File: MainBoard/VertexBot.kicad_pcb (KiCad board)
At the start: 2 copper layers, 115.6 x 107.8 mm, 70 parts, among them J1 Battery, J2 I2C Extension, J4 Left Motor, J5 Right Motor, J6 Led Strip, Q1 BSS138, Q2 BSS138, Q3 BSS138, SW1 SW_SPST, U1 DRV8830DGQR, U10 MAX4466 (LEFT), U11 MAX4466 (RIGHT), U12 ESP32-S3-CAM-B, U13 ESP32-S3-CAM-A, U14 MAX98357A, U2 DRV8830DGQR, U3 S13V30F5, U5 INMP441, U6 0.96 INCH OLED, U7 DRV5033AJxLPG, U8 DRV5033AJxLPG, U9 MPU 6050

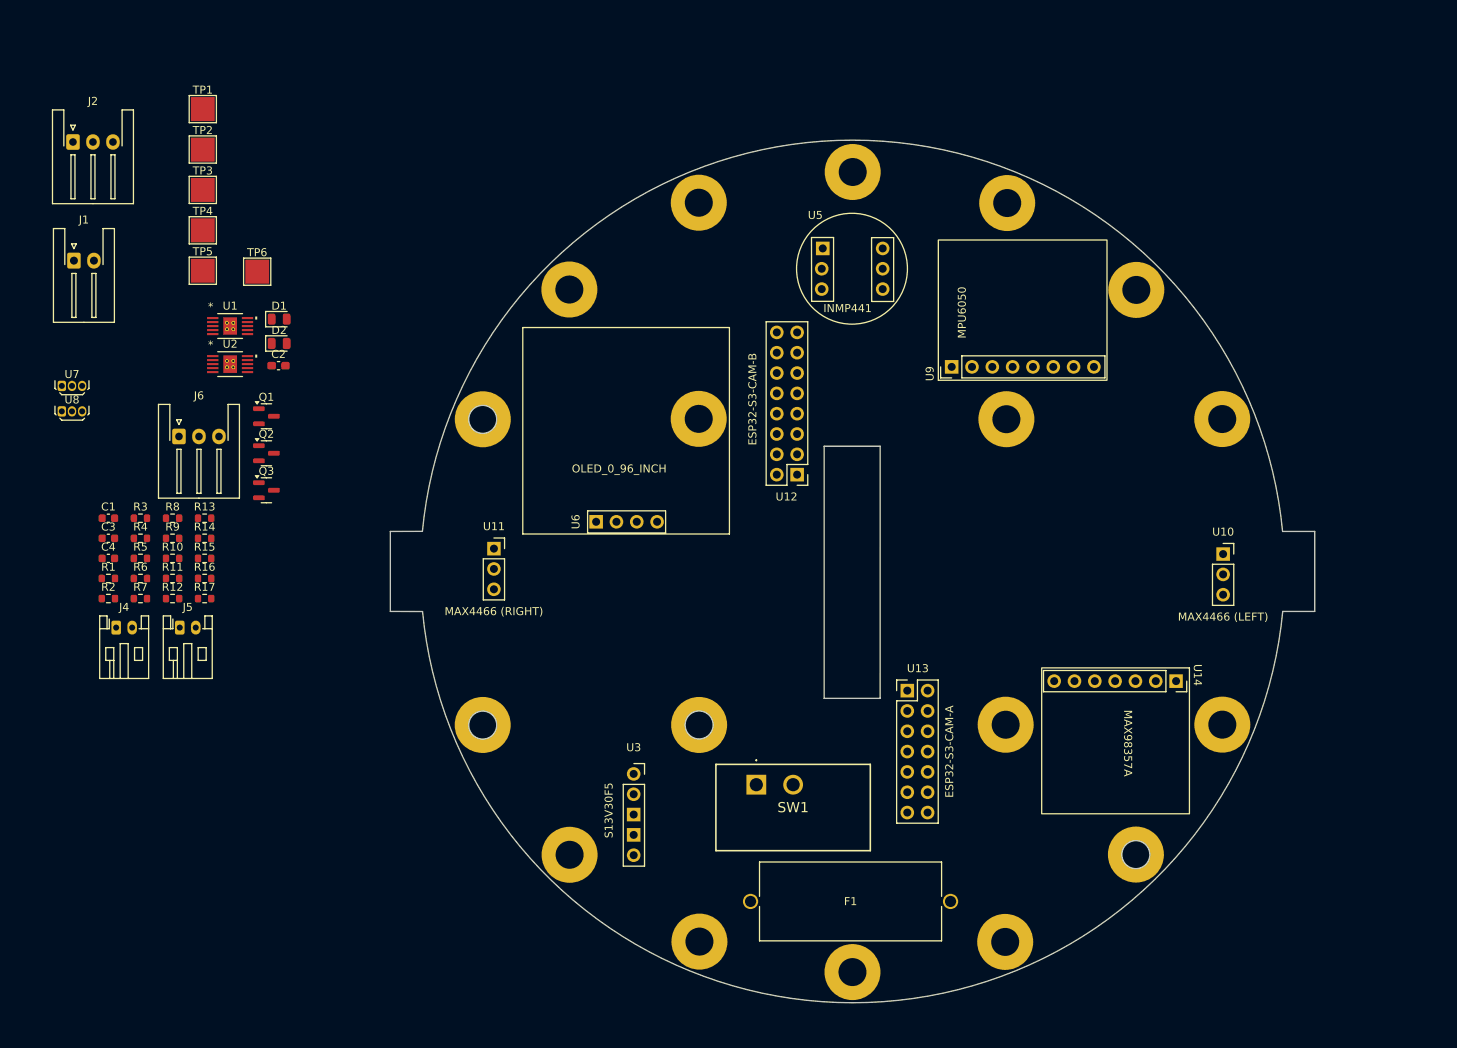
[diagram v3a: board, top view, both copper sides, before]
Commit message: Adjust DRV8830DGQR to allow thermal pad connect to GND Adjust some of the modules courtyard Fix mounting holes symbols to have connection
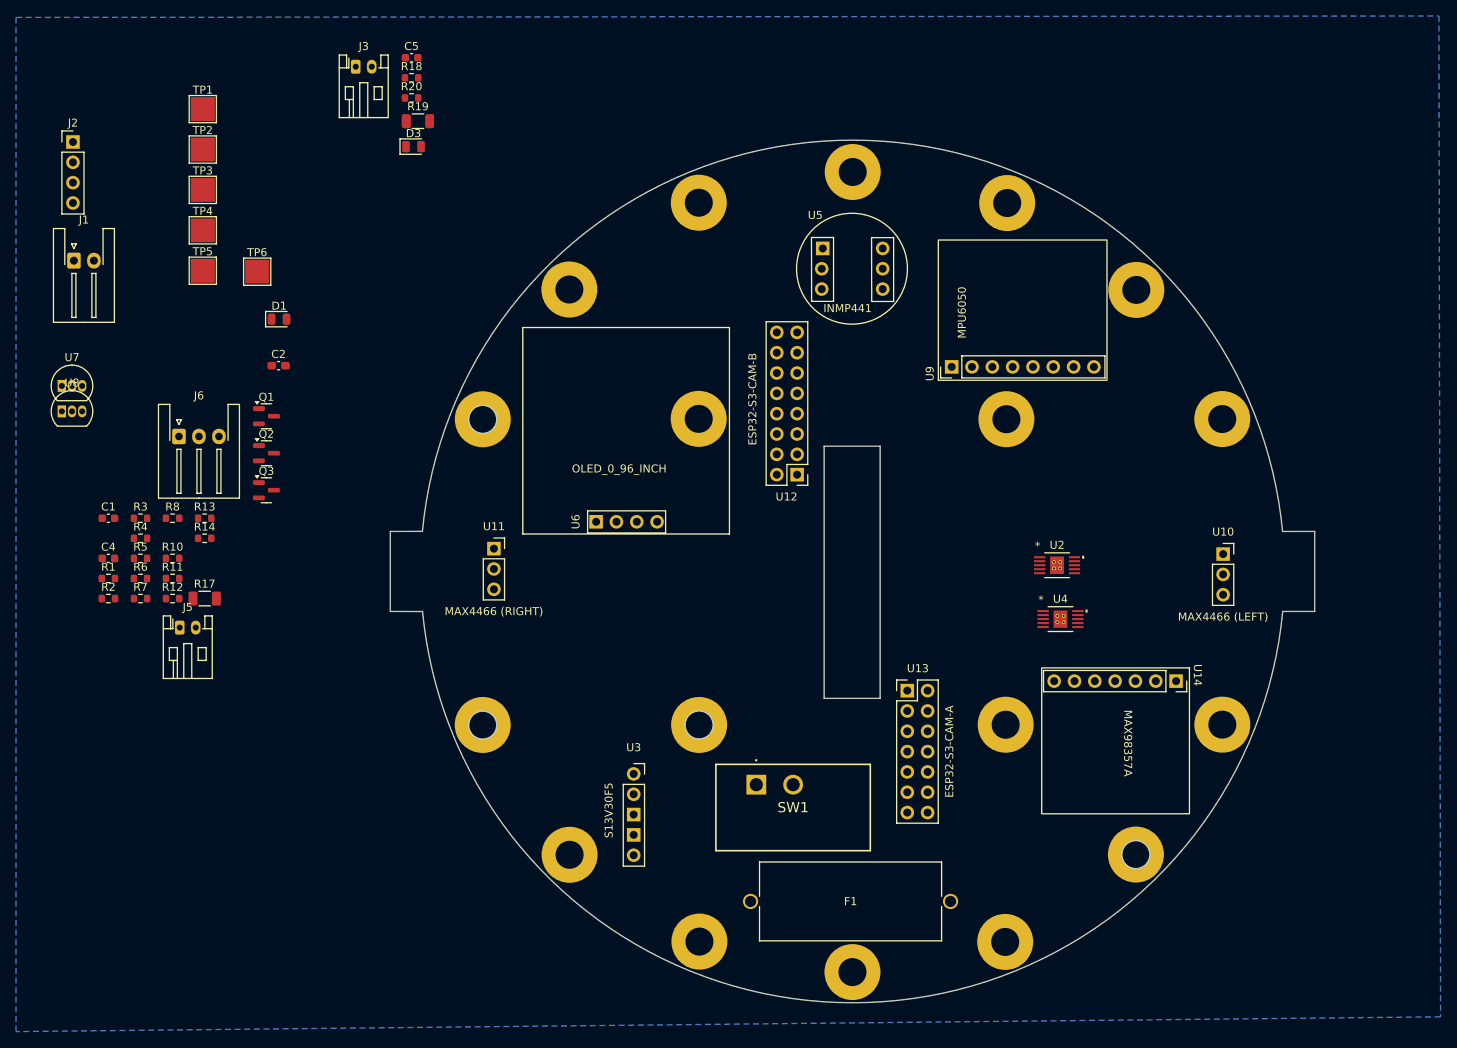
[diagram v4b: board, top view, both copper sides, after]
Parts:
- removed C3: 100nF, Capacitor_SMD:C_0603_1608Metric
- removed D2: LED, LED_SMD:LED_0805_2012Metric
- removed J4: Left Motor, Connector_JST:JST_PH_S2B-PH-K_1x02_P2.00mm_Horizontal
- removed R15: 1K, Resistor_SMD:R_0603_1608Metric
- removed R16, R9: 0.44, Resistor_SMD:R_0603_1608Metric
- removed U1: DRV8830DGQR, Vertex_Bot:DGQ10_2P18X1P72
- added C5: 100nF, Capacitor_SMD:C_0603_1608Metric, F.Cu at (65.1, 25.2)
- added D3: LED, LED_SMD:LED_0805_2012Metric, F.Cu at (65.4, 36.3)
- added J3: Right Motor, Connector_JST:JST_PH_S2B-PH-K_1x02_P2.00mm_Horizontal, F.Cu at (58.2, 26.3)
- added R18: 0.44, Resistor_SMD:R_0603_1608Metric, F.Cu at (65.1, 27.7)
- added R19: 0.44, Resistor_SMD:R_1206_3216Metric, F.Cu at (65.9, 33.1)
- added R20: 1K, Resistor_SMD:R_0603_1608Metric, F.Cu at (65.1, 30.2)
- added U4: DRV8830DGQR, Vertex_Bot:DGQ10_2P18X1P72, F.Cu at (146.2, 95.4)
- J2: footprint Connector_JST:JST_XH_S3B-XH-A-1_1x03_P2.50mm_Horizontal -> Connector_PinHeader_2.54mm:PinHeader_1x04_P2.54mm_Vertical
- R17: footprint Resistor_SMD:R_0603_1608Metric -> Resistor_SMD:R_1206_3216Metric
- U7, U8: footprint Package_TO_SOT_THT:TO-92Flat -> Package_TO_SOT_THT:TO-92_Inline
- moved U2 106.4 mm to (145.8, 88.7)
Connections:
- H1 pad 1: (no net) -> GND
- H10 pad 1: (no net) -> GND
- H11 pad 1: (no net) -> GND
- H12 pad 1: (no net) -> GND
- H13 pad 1: (no net) -> GND
- H14 pad 1: (no net) -> GND
- H15 pad 1: (no net) -> GND
- H16 pad 1: (no net) -> GND
- H17 pad 1: (no net) -> GND
- H18 pad 1: (no net) -> GND
- H2 pad 1: (no net) -> GND
- H3 pad 1: (no net) -> GND
- H4 pad 1: (no net) -> GND
- H5 pad 1: (no net) -> GND
- H6 pad 1: (no net) -> GND
- H7 pad 1: (no net) -> GND
- H8 pad 1: (no net) -> GND
- H9 pad 1: (no net) -> GND
- U2 pad V: (no net) -> GND
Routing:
- added copper zone on B.Cu, net GND

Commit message: Completed Main PCB first draft (v0.1)
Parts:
- removed R18, R8: 0.44, Resistor_SMD:R_0603_1608Metric
- C1, C4, C5: footprint Capacitor_SMD:C_0603_1608Metric -> Capacitor_SMD:C_0603_1608Metric_Pad1.08x0.95mm_HandSolder
- D1, D3: footprint LED_SMD:LED_0805_2012Metric -> LED_SMD:LED_0805_2012Metric_Pad1.15x1.40mm_HandSolder
- F1, J5, U14: moved to B.Cu
- J1: footprint Connector_JST:JST_XH_S2B-XH-A-1_1x02_P2.50mm_Horizontal -> Connector_BarrelJack:BarrelJack_Kycon_KLDX-0202-xC_Horizontal; moved to B.Cu
- J3: value Right Motor -> Left Motor; moved to B.Cu
- J6: footprint Connector_JST:JST_XH_S3B-XH-A-1_1x03_P2.50mm_Horizontal -> Connector_JST:JST_PH_B3B-PH-K_1x03_P2.00mm_Vertical
- R1, R10, R11, R12, R13, R14, R2, R20, R3, R4, R5, R6, R7: footprint Resistor_SMD:R_0603_1608Metric -> Resistor_SMD:R_0603_1608Metric_Pad0.98x0.95mm_HandSolder
- R17, R19: value 0.44 -> 0.22; footprint Resistor_SMD:R_1206_3216Metric -> Resistor_SMD:R_2512_6332Metric_Pad1.40x3.35mm_HandSolder
- U10, U11: footprint Connector_PinSocket_2.54mm:PinSocket_1x03_P2.54mm_Vertical -> Vertex_Bot:MAX4466_VERTICAL
- U3: footprint Vertex_Bot:S13V30F5_VERTICAL -> Vertex_Bot:S13V30F5_HORIZONTAL; moved to B.Cu
- U7, U8: footprint Package_TO_SOT_THT:TO-92_Inline -> Package_TO_SOT_THT:TO-92Flat; moved to B.Cu
- moved U7 155.6 mm to (175.5, 88.3), turned to -90 degrees
- moved C1 144.1 mm to (171.1, 91.2)
- moved J1 142.4 mm to (152.3, 110.2), turned to 145 degrees
- moved TP4 137.8 mm to (167.8, 95.7)
- moved R12 136.0 mm to (171.1, 88.4)
- moved C5 127.1 mm to (147.4, 122.1), turned to 90 degrees
- moved TP2 116.7 mm to (138.3, 98.1)
- moved R20 115.5 mm to (136.8, 120.8), turned to -90 degrees
- moved R19 114.6 mm to (143.1, 117.8)
- moved J5 113.8 mm to (146.0, 126.5), turned to -146.5 degrees
- moved J3 108.0 mm to (96.2, 127.5), turned to 149 degrees
- moved D3 107.4 mm to (136.7, 116.6), turned to -90 degrees
- moved TP1 106.2 mm to (104.6, 115.2)
- moved R5 105.4 mm to (136.7, 89.1)
- moved R7 105.4 mm to (136.7, 92.2)
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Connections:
- net Net-(SW1-B) renamed SWITCH
- net Net-(U3-VIN) renamed Vin
- J1 pad 2: Net-(J1-Pin_2) -> Vbat
- SW1 pad 1: Net-(J1-Pin_2) -> Vbat
- TP1 pad 1: Net-(J1-Pin_2) -> Vbat
- U2 pad 1: Net-(J5-Pin_1) -> Net-(J3-Pin_1)
- U2 pad 3: Net-(J5-Pin_2) -> Net-(J3-Pin_2)
- U4 pad 1: Net-(J3-Pin_1) -> Net-(J5-Pin_1)
- U4 pad 3: Net-(J3-Pin_2) -> Net-(J5-Pin_2)
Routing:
- net 5V: track 0.00 -> 286.6 mm, vias 0 -> 6
- net 3.3V-A: track 0.00 -> 229.7 mm, vias 0 -> 10
- net SCL: track 0.00 -> 212.3 mm, vias 0 -> 11
- net SDA: track 0.00 -> 210.3 mm, vias 0 -> 12
- net 3.3V-B: track 0.00 -> 94.9 mm, vias 0 -> 3
- net RIGHT_WHEEL: track 0.00 -> 93.1 mm, vias 0 -> 2
- net LEFT_WHEEL: track 0.00 -> 67.7 mm
- net TX: track 0.00 -> 67.3 mm, vias 0 -> 2
- net RX: track 0.00 -> 66.5 mm, vias 0 -> 2
- net Vbat: track 0.00 -> 62.0 mm
- net INT: track 0.00 -> 60.4 mm
- net SYNC: track 0.00 -> 53.9 mm, vias 0 -> 2
- net Vin: track 0.00 -> 47.8 mm
- net GND: track 0.00 -> 47.3 mm, vias 0 -> 6
- net MIC_B: track 0.00 -> 45.0 mm
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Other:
- outline, holes or cut-outs redrawn

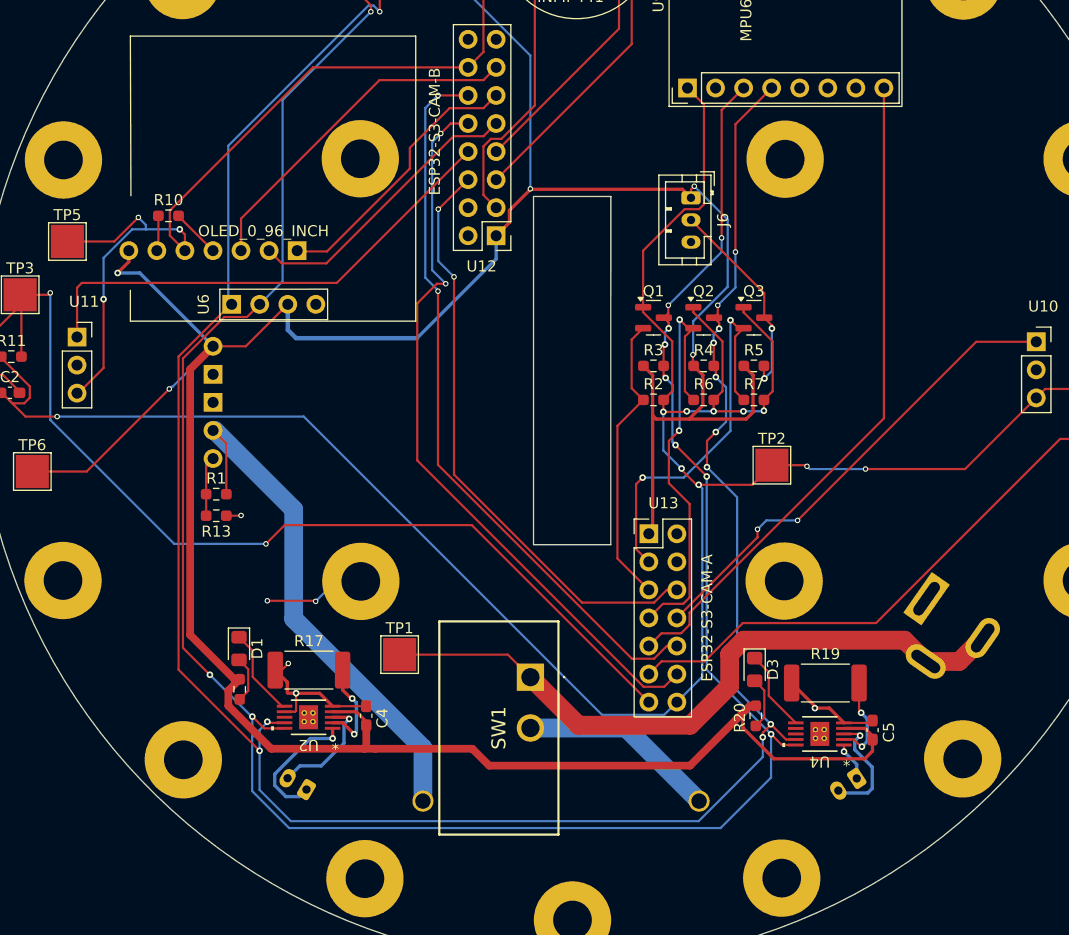
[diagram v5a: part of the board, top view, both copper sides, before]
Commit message: Reviewed power requirements, adjusted power track widths Changed to DC barel connector with proper current rating Added corresponding symbol, footprint and 3D model
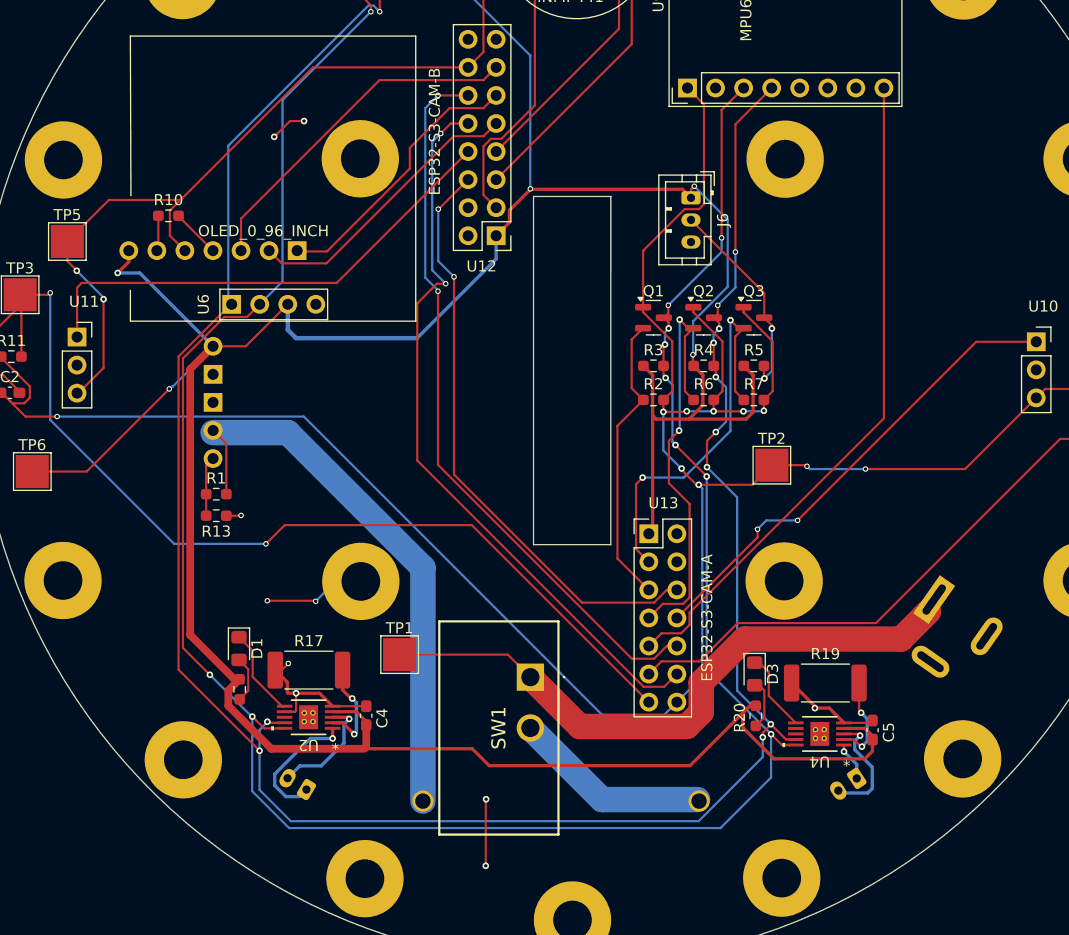
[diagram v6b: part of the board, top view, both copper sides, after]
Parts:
- removed J1: Battery, Connector_BarrelJack:BarrelJack_Kycon_KLDX-0202-xC_Horizontal
- added J4: 694106301002, Connector_THT_Wurth:J_Wurth_WR-DC_694106301002, B.Cu at (153.0, 110.3)
- moved D3 0.41 mm to (136.7, 117.0)
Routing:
- net GND: track 47.3 -> 56.6 mm, vias 6 -> 10
- net Vbat: track 62.0 -> 56.5 mm
- net 3.3V-B: track 94.9 -> 90.8 mm, vias 3 -> 2
- net Vin: track 47.8 -> 51.7 mm

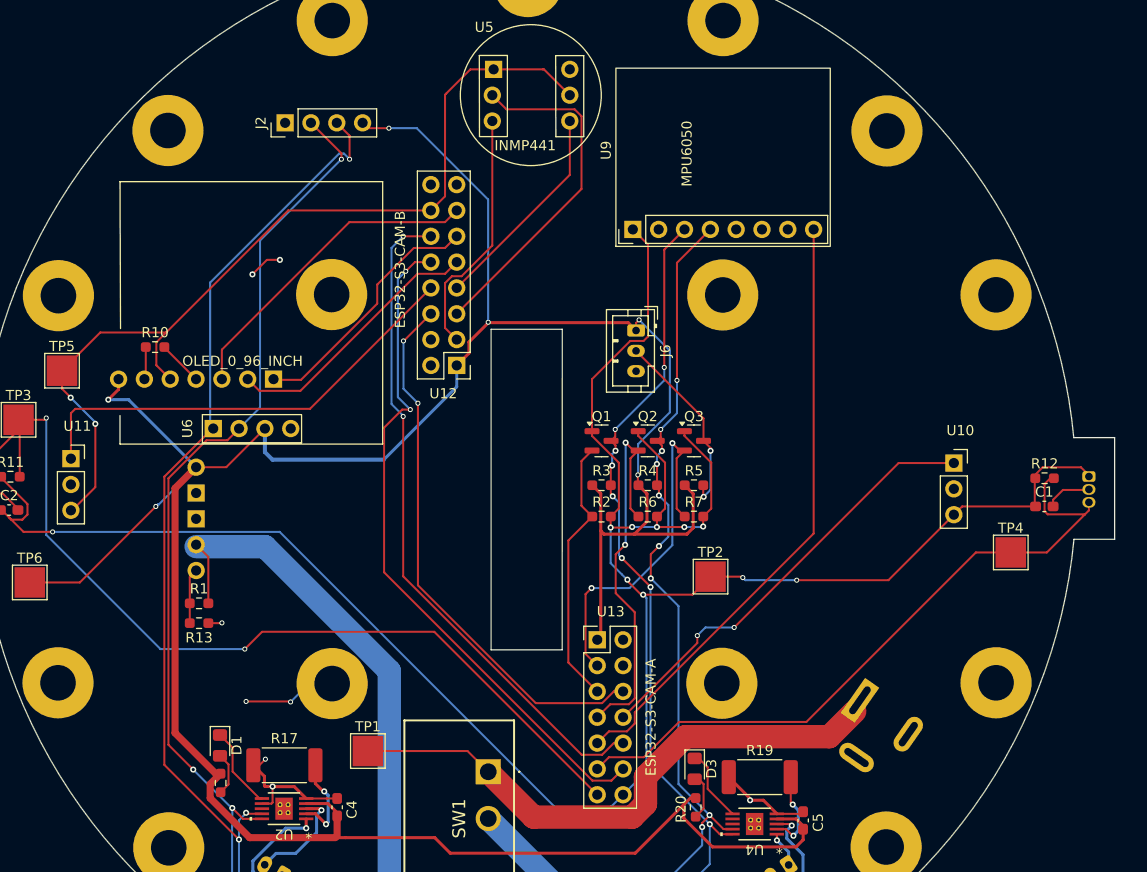
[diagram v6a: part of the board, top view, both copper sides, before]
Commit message: Add 3D models for MPU3050, MAX98357, OLED Review MAX footprint placements to keep away from booster
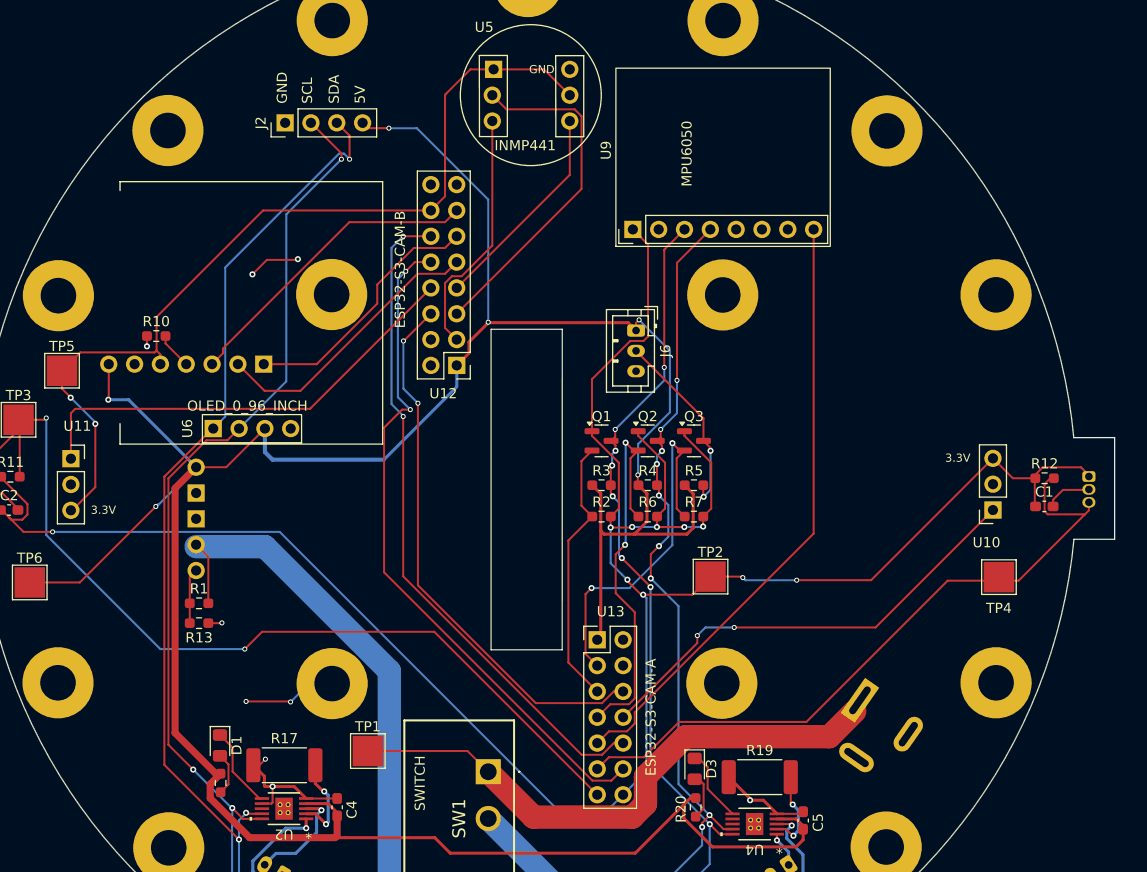
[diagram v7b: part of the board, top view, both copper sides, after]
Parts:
- moved U10 6.01 mm to (166.1, 91.6), turned to 180 degrees
- moved TP4 2.69 mm to (166.7, 98.2)
- moved U14 1.76 mm to (95.1, 78.0)
- moved R10 1.09 mm to (83.8, 74.4)
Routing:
- net 3.3V-A: track 229.7 -> 232.7 mm
- net MIC_A: track 43.3 -> 45.5 mm
- net 3.3V-B: track 90.8 -> 88.7 mm
- net AMP_BCLK: track 26.3 -> 27.9 mm
- net AMP_DOUT: track 31.7 -> 30.6 mm
- net 5V: track 286.5 -> 287.6 mm
- net AMP_LRCLK: track 24.5 -> 25.3 mm
- net GND: track 56.6 -> 56.2 mm, vias 10 -> 11
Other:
- board text added: "3.3V"
- board text added: "5V"
- board text added: "FUSE HOLDER"
- board text added: "GND"
- board text added: "SCL"
- board text added: "SDA"
- board text added: "SWITCH"

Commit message: Move MAX4466 (analog mics) away from USP connectors All 3D models update Add silkscreen user labels
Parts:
- U10, U11: footprint Vertex_Bot:MAX4466_VERTICAL -> Vertex_Bot:MAX4466_HORIZONTAL
- moved TP1 34.8 mm to (132.1, 136.5)
- moved U11 31.9 mm to (93.4, 112.8), turned to 180 degrees
- moved U10 24.9 mm to (147.0, 107.7), turned to 0 degrees
- moved D1 4.55 mm to (92.1, 118.8)
- moved R17 3.77 mm to (100.1, 116.4)
- moved R19 0.26 mm to (142.9, 117.8)
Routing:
- net 3.3V-B: track 88.7 -> 117.7 mm, vias 2 -> 1
- net MIC_A: track 45.5 -> 25.0 mm
- net 3.3V-A: track 232.7 -> 249.0 mm, vias 10 -> 11
- net Vbat: track 56.5 -> 69.9 mm
- net MIC_B: track 45.0 -> 51.5 mm
- net Net-(D1-K): track 8.66 -> 3.75 mm
- net 5V: track 287.6 -> 290.9 mm
- net Net-(D1-A): track 4.25 -> 2.19 mm
- net Net-(U2-ISENSE): track 8.84 -> 9.92 mm
- net GND: track 56.2 -> 55.9 mm, vias 11 -> 10
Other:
- board text added: "Counter Left"
- board text added: "Counter Right"
- board text added: "VBAT"
